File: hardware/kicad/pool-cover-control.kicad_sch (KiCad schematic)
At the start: 0 parts

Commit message: feat(hardware): add custom SLA-12VDC-SL-C symbol and footprint
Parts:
- added D1: D_Schottky, symbol Device:D_Schottky
- added Q1: Q_PMOS_GDS, Package_TO_SOT_SMD:TO-252-3_TabPin2, symbol Device:Q_PMOS_GDS
- added RL1: SLA-12VDC-SL-C, pool-cover-control:SLA-12VDC-SL-C, symbol pool-cover-control:SLA-12VDC-SL-C
- added U1: STM32G031K8Tx, Package_QFP:LQFP-32_7x7mm_P0.8mm, symbol MCU_ST_STM32G0:STM32G031K8Tx
- added U2: ULN2003A, symbol Transistor_Array:ULN2003A
- added U3: AMS1117-3.3, Package_TO_SOT_SMD:SOT-223-3_TabPin2, symbol Regulator_Linear:AMS1117-3.3
- added U4: PC817, Package_SO:SOP-4_4.4x2.6mm_P1.27mm, symbol Isolator:PC817

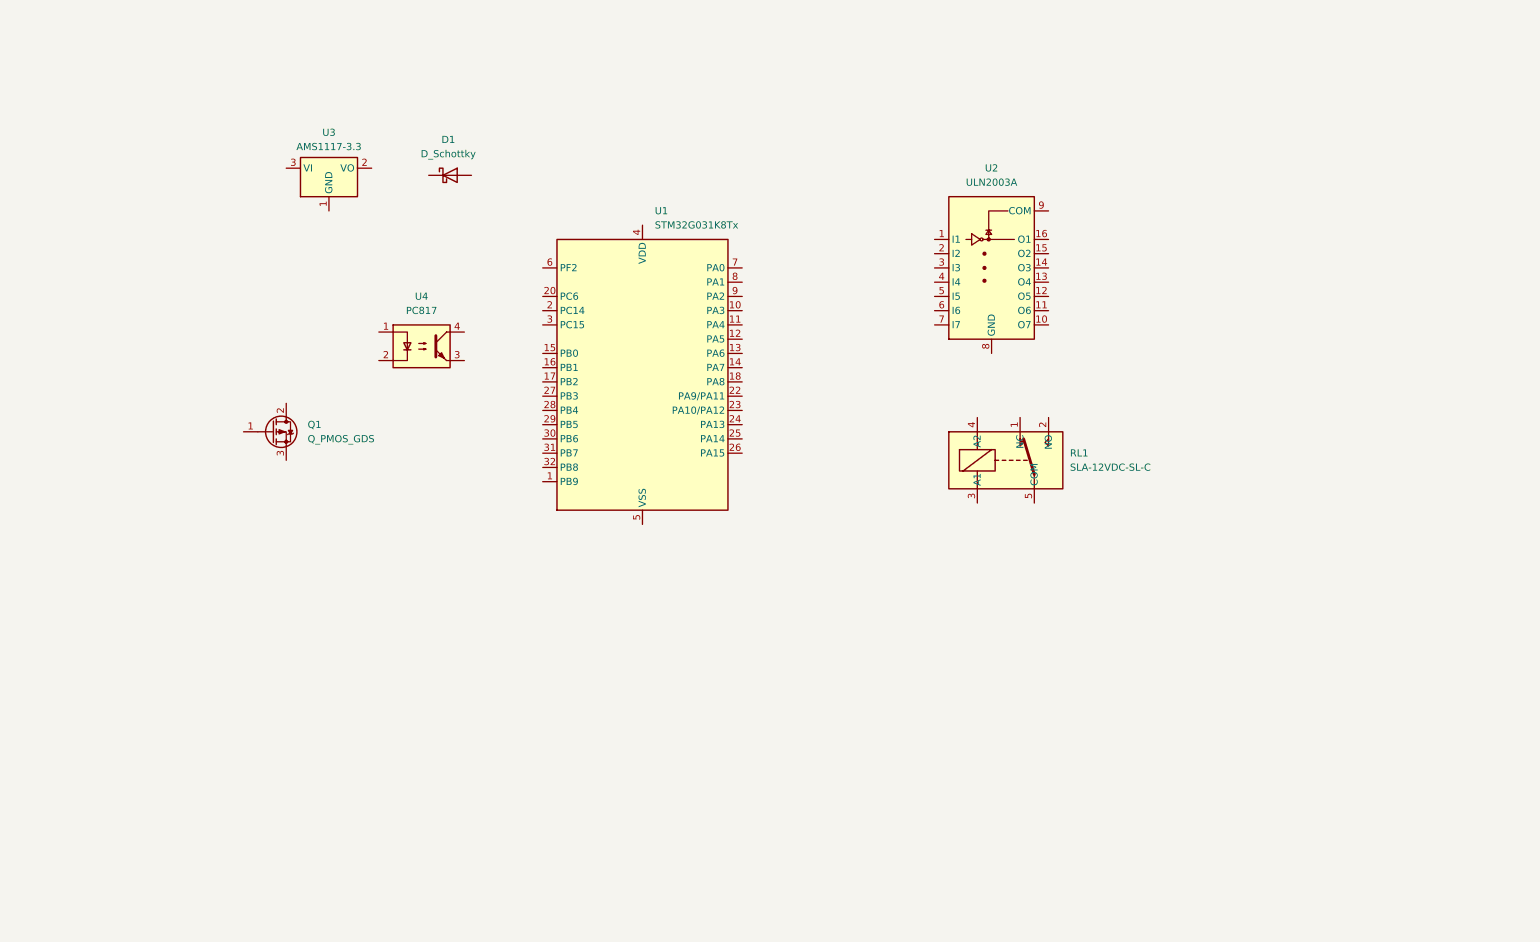
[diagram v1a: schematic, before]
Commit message: feat(hardware): implement SC1 power tree schematic
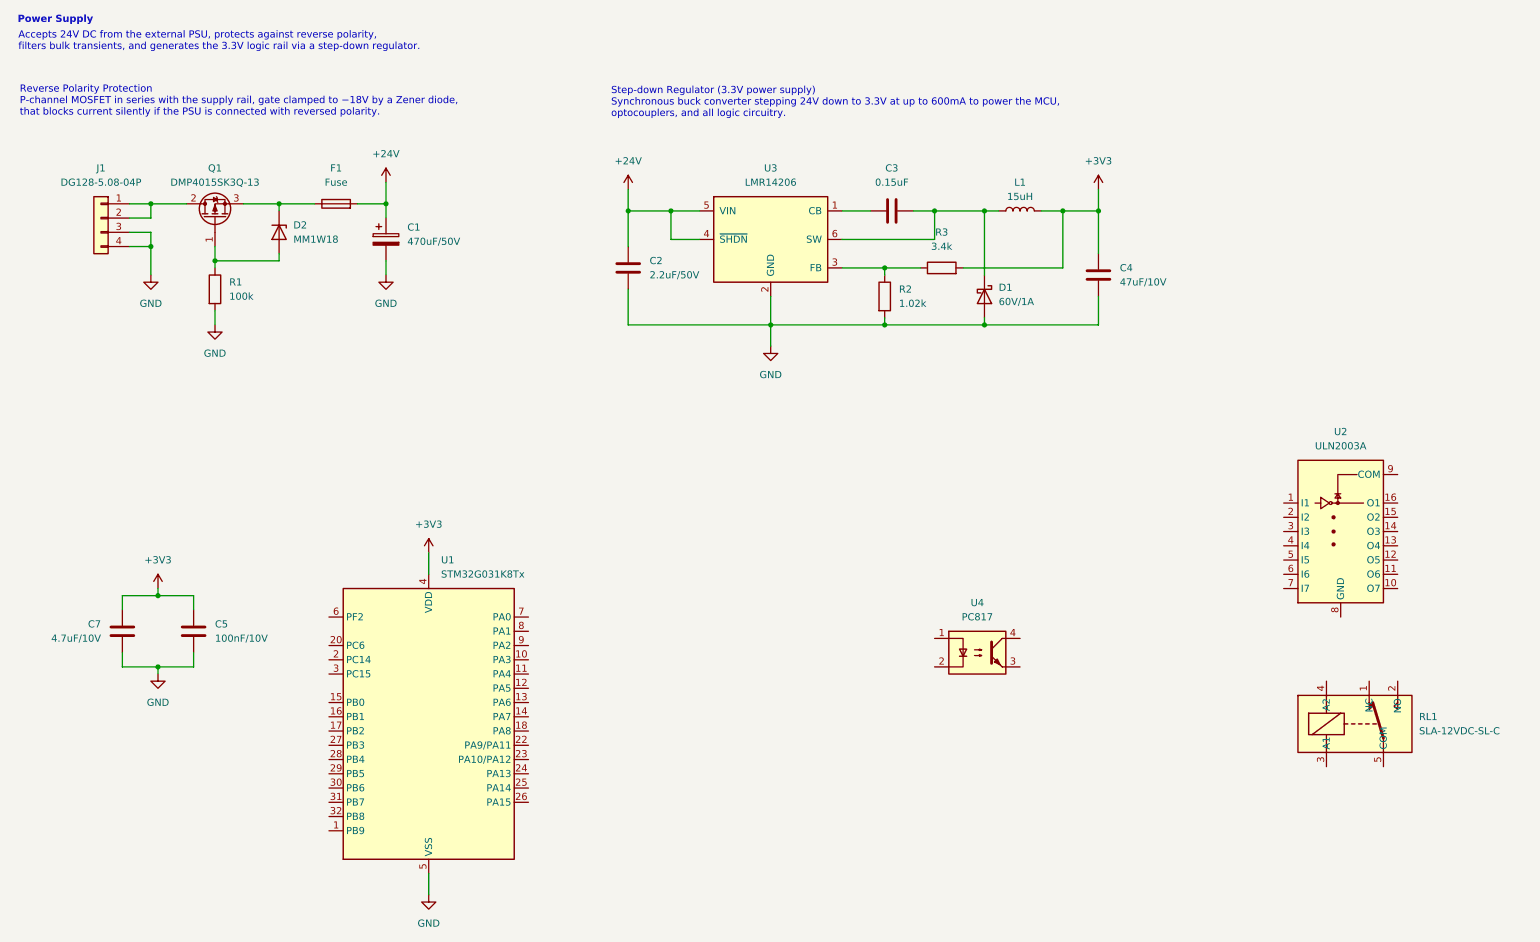
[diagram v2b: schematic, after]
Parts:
- removed U3: AMS1117-3.3, Package_TO_SOT_SMD:SOT-223-3_TabPin2, symbol Regulator_Linear:AMS1117-3.3
- added C1: 470uF/50V, Capacitor_THT:C_Radial_D10.0mm_H20.0mm_P5.00mm, symbol Device:C_Polarized
- added C2: 2.2uF/50V, Capacitor_SMD:C_0805_2012Metric, symbol Device:C
- added C3: 0.15uF, Capacitor_SMD:C_0603_1608Metric, symbol Device:C
- added C4: 47uF/10V, Capacitor_SMD:C_0805_2012Metric, symbol Device:C
- added C5: 100nF/10V, Capacitor_SMD:C_0805_2012Metric, symbol Device:C
- added C7: 4.7uF/10V, Capacitor_SMD:C_0805_2012Metric, symbol Device:C
- added D2: MM1W18, Diode_SMD:D_SOD-123, symbol Device:D_Zener
- added F1: Fuse, Fuse:Fuseholder_Blade_Mini_Keystone_3568, symbol Device:Fuse
- added J1: DG128-5.08-04P, Connector_Phoenix_MSTB:PhoenixContact_MSTBVA_2,5_4-G-5,08_1x04_P5.08mm_Vertical, symbol Connector_Generic:Conn_01x04
- added L1: 15uH, Inductor_SMD:L_Bourns_SRP7028A_7.3x6.6mm, symbol Device:L
- added R1: 100k, Resistor_SMD:R_0402_1005Metric, symbol Device:R
- added R2: 1.02k, Resistor_SMD:R_0402_1005Metric, symbol Device:R
- added R3: 3.4k, Resistor_SMD:R_0402_1005Metric, symbol Device:R
- added U3: LMR14206, Package_TO_SOT_SMD:SOT-23-6, symbol Regulator_Switching:LMR14206
- D1: value D_Schottky -> 60V/1A; footprint (none) -> Diode_SMD:D_SMA
- Q1: value Q_PMOS_GDS -> DMP4015SK3Q-13
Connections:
- net at Q1.1 (G): now also D2.2 (A), R1.1
- net at Q1.2 (D): now also J1.1 (Pin_1), J1.2 (Pin_2)
- net at Q1.3 (S): now also D2.1 (K), F1.1
- net at D1.1 (K): now also C3.2, L1.1, U3.6 (SW)
- net GND: now reaches D1.2 (A)
- net GND: now also U1.5 (VSS), C1.2, C2.1, C4.1, C5.1, C7.1, J1.3 (Pin_3), J1.4 (Pin_4), R1.2, R2.2, U3.2 (GND)
- net +3V3: now reaches U1.4 (VDD)
- net +3V3: now also C4.2, C5.2, C7.2, L1.2, R3.2
- new net: R2.1, R3.1, U3.3 (FB)
- new net: C3.1, U3.1 (CB)
- new net +24V: C1.1, C2.2, F1.2, U3.4 (~{SHDN}), U3.5 (VIN)
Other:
- note added: "Accepts 24V DC from the external PSU, protects against reverse polarity, filters bulk transients, and generates the 3.3V logic rail via a step-down regulator."
- note added: "Power Supply"
- note added: "Reverse Polarity Protection P-channel MOSFET in series with the supply rail, gate clamped to −18V by a Zener diode, that blocks current silently if the PSU is connected with reversed polarity."
- note added: "Step-down Regulator (3.3V power supply) Synchronous buck converter stepping 24V down to 3.3V at up to 600mA to power the MCU, optocouplers, and all logic circuitry."
- moved on the sheet: Q1, RL1, U1, U2, U4
